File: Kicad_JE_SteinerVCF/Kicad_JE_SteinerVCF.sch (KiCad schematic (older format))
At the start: 36 parts

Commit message: Initial complete RevA sch
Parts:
- added C5: 1u, symbol Device:C
- added C6: 10u, symbol Device:CP
- added Q1: BC559, Package_TO_SOT_THT:TO-92_Inline, symbol Transistor_BJT:BC559
- added Q2: BC549, Package_TO_SOT_THT:TO-92_Inline, symbol Transistor_BJT:BC549
- added R2: 82k, symbol Device:R
- added R3: 3M3, symbol Device:R
- added R4: 18k, symbol Device:R
- added R5: 1k, symbol Device:R
- added R6, R7: 2k, symbol Device:R
- added RV3: 25k, symbol Device:R_POT_TRIM
- RV1: renamed from RV?; value R_POT -> 1k
- gave numbers to parts that had none: 30
- renumbered C3 to C2, C4 to C3, C2 to C4
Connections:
- wire segments 103 -> 135
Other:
- note added: "Driver"
- note added: "Q Adj"

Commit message: SMD sub sheet
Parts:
- added C?: CP, symbol Device:CP
- added P?: Doepfer_Power_10pin, Connectors_IDC:IDC-Header_2x05_Pitch2.54mm_Straight, symbol Eurorack:Doepfer_Power_10pin
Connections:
- wire segments 135 -> 160

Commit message: ERC, Footprints and Annotation in SCH
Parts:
- C101: renamed from C1; footprint (none) -> Capacitor_THT:C_Rect_L7.0mm_W2.0mm_P5.00mm
- C102: renamed from C2; footprint (none) -> Capacitor_THT:CP_Radial_D10.0mm_P5.00mm
- C103: renamed from C3; footprint (none) -> Capacitor_THT:CP_Radial_D10.0mm_P5.00mm
- C104: renamed from C4; footprint (none) -> Capacitor_THT:C_Rect_L7.0mm_W2.0mm_P5.00mm
- C105: renamed from C?; footprint (none) -> Capacitor_THT:CP_Radial_D10.0mm_P5.00mm
- C106: renamed from C5; footprint (none) -> Capacitor_THT:C_Rect_L7.0mm_W2.0mm_P5.00mm
- C107: renamed from C6; footprint (none) -> Capacitor_THT:CP_Radial_D10.0mm_P3.80mm
- C108: renamed from C7; footprint (none) -> Capacitor_THT:C_Rect_L7.0mm_W2.0mm_P5.00mm
- C109: renamed from C8; footprint (none) -> Capacitor_THT:C_Rect_L7.0mm_W2.0mm_P5.00mm
- C110: renamed from C9; footprint (none) -> Capacitor_THT:C_Rect_L7.0mm_W2.0mm_P5.00mm
- C111: renamed from C10; footprint (none) -> Capacitor_THT:CP_Radial_D10.0mm_P5.00mm
- J101: renamed from J1; footprint (none) -> AJ-Dropbox-Kicad:PJ301SM
- J102: renamed from J2; footprint (none) -> AJ-Dropbox-Kicad:PJ301SM
- J103: renamed from J3; footprint (none) -> AJ-Dropbox-Kicad:PJ301SM
- J104: renamed from J4; footprint (none) -> AJ-Dropbox-Kicad:PJ301SM
- J105: renamed from J5; footprint (none) -> AJ-Dropbox-Kicad:PJ301SM
- R101: renamed from R1; footprint (none) -> Resistor_THT:R_Axial_DIN0309_L9.0mm_D3.2mm_P12.70mm_Horizontal
- R102: renamed from R2; footprint (none) -> Resistor_THT:R_Axial_DIN0309_L9.0mm_D3.2mm_P12.70mm_Horizontal
- R103: renamed from R3; footprint (none) -> Resistor_THT:R_Axial_DIN0309_L9.0mm_D3.2mm_P12.70mm_Horizontal
- R104: renamed from R4; footprint (none) -> Resistor_THT:R_Axial_DIN0309_L9.0mm_D3.2mm_P12.70mm_Horizontal
- R105: renamed from R5; footprint (none) -> Resistor_THT:R_Axial_DIN0309_L9.0mm_D3.2mm_P12.70mm_Horizontal
- R106: renamed from R6; footprint (none) -> Resistor_THT:R_Axial_DIN0309_L9.0mm_D3.2mm_P12.70mm_Horizontal
- R107: renamed from R7; footprint (none) -> Resistor_THT:R_Axial_DIN0309_L9.0mm_D3.2mm_P12.70mm_Horizontal
- R108: renamed from R8; footprint (none) -> Resistor_THT:R_Axial_DIN0309_L9.0mm_D3.2mm_P12.70mm_Horizontal
- R109: renamed from R9; footprint (none) -> Resistor_THT:R_Axial_DIN0309_L9.0mm_D3.2mm_P12.70mm_Horizontal
- R110: renamed from R10; footprint (none) -> Resistor_THT:R_Axial_DIN0309_L9.0mm_D3.2mm_P12.70mm_Horizontal
- R111: renamed from R11; footprint (none) -> Resistor_THT:R_Axial_DIN0309_L9.0mm_D3.2mm_P12.70mm_Horizontal
- R112: renamed from R12; footprint (none) -> Resistor_THT:R_Axial_DIN0309_L9.0mm_D3.2mm_P12.70mm_Horizontal
- R113: renamed from R13; footprint (none) -> Resistor_THT:R_Axial_DIN0309_L9.0mm_D3.2mm_P12.70mm_Horizontal
- R114: renamed from R14; footprint (none) -> Resistor_THT:R_Axial_DIN0309_L9.0mm_D3.2mm_P12.70mm_Horizontal
- R115: renamed from R15; footprint (none) -> Resistor_THT:R_Axial_DIN0309_L9.0mm_D3.2mm_P12.70mm_Horizontal
- R116: renamed from R16; footprint (none) -> Resistor_THT:R_Axial_DIN0309_L9.0mm_D3.2mm_P12.70mm_Horizontal
- R117: renamed from R17; footprint (none) -> Resistor_THT:R_Axial_DIN0309_L9.0mm_D3.2mm_P12.70mm_Horizontal
- RV101: renamed from RV1; footprint (none) -> Potentiometer_THT:Potentiometer_Alps_RK09K_Single_Vertical
- RV102: renamed from RV2; footprint (none) -> Potentiometer_THT:Potentiometer_Alps_RK09K_Single_Vertical
- RV103: renamed from RV3; footprint (none) -> Potentiometer_THT:Potentiometer_Alps_RK09K_Single_Vertical
- gave numbers to parts that had none: 1
- renumbered D1 to D101, D2 to D102, D3 to D103, D4 to D104, D5 to D105, D6 to D106, D7 to D107, D8 to D108, Q1 to Q101, Q2 to Q102, Q3 to Q103, Q4 to Q104

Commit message: SMD section routed RevA
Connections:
- net labels added: +10V
- net labels removed: VCC
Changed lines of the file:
@@
 	0    1    1    0
-$EndComp
-$Comp
-L power:VCC #PWR0102
-U 1 1 5C434C5C
-P 4700 700
-F 0 "#PWR0102" H 4700 550 50  0001 C CNN
-F 1 "VCC" H 4717 873 50  0000 C CNN
-F 2 "" H 4700 700 50  0001 C CNN
-F 3 "" H 4700 700 50  0001 C CNN
-	1    4700 700
-	1    0    0    -1
 $EndComp
 Wire Wire Line
@@
 Wire Wire Line
 	2000 4850 2000 4750
-$Comp
-L power:VCC #PWR0109
-U 1 1 5C446275
-P 2000 4400
-F 0 "#PWR0109" H 2000 4250 50  0001 C CNN
-F 1 "VCC" H 2017 4573 50  0000 C CNN
-F 2 "" H 2000 4400 50  0001 C CNN
-F 3 "" H 2000 4400 50  0001 C CNN
-	1    2000 4400
-	1    0    0    -1
-$EndComp
 Wire Wire Line
 	2000 4450 2000 4400
@@
 F 3 "http://www.fairchildsemi.com/ds/BC/BC547.pdf" H 3350 2450 50  0001 L CNN
 	1    3350 2450
-	1    0    0    -1
-$EndComp
-$Comp
-L power:VCC #PWR0106
-U 1 1 5C480942
-P 2800 1800
-F 0 "#PWR0106" H 2800 1650 50  0001 C CNN
-F 1 "VCC" H 2817 1973 50  0000 C CNN
-F 2 "" H 2800 1800 50  0001 C CNN
-F 3 "" H 2800 1800 50  0001 C CNN
-	1    2800 1800
 	1    0    0    -1
 $EndComp
@@
 $EndComp
 Connection ~ 2450 1400
+$Comp
+L power:+10V #PWR0102
+U 1 1 5C60D9FE
+P 2000 4400
+F 0 "#PWR0102" H 2000 4250 50  0001 C CNN
+F 1 "+10V" H 2015 4573 50  0000 C CNN
+F 2 "" H 2000 4400 50  0001 C CNN
+F 3 "" H 2000 4400 50  0001 C CNN
+	1    2000 4400
+	1    0    0    -1
+$EndComp
+$Comp
+L power:+10V #PWR0106
+U 1 1 5C60DB41
+P 4700 700
+F 0 "#PWR0106" H 4700 550 50  0001 C CNN
+F 1 "+10V" H 4715 873 50  0000 C CNN
+F 2 "" H 4700 700 50  0001 C CNN
+F 3 "" H 4700 700 50  0001 C CNN
+	1    4700 700
+	1    0    0    -1
+$EndComp
+$Comp
+L power:+10V #PWR0109
+U 1 1 5C60DF5D
+P 2800 1800
+F 0 "#PWR0109" H 2800 1650 50  0001 C CNN
+F 1 "+10V" H 2815 1973 50  0000 C CNN
+F 2 "" H 2800 1800 50  0001 C CNN
+F 3 "" H 2800 1800 50  0001 C CNN
+	1    2800 1800
+	1    0    0    -1
+$EndComp
 $EndSCHEMATC

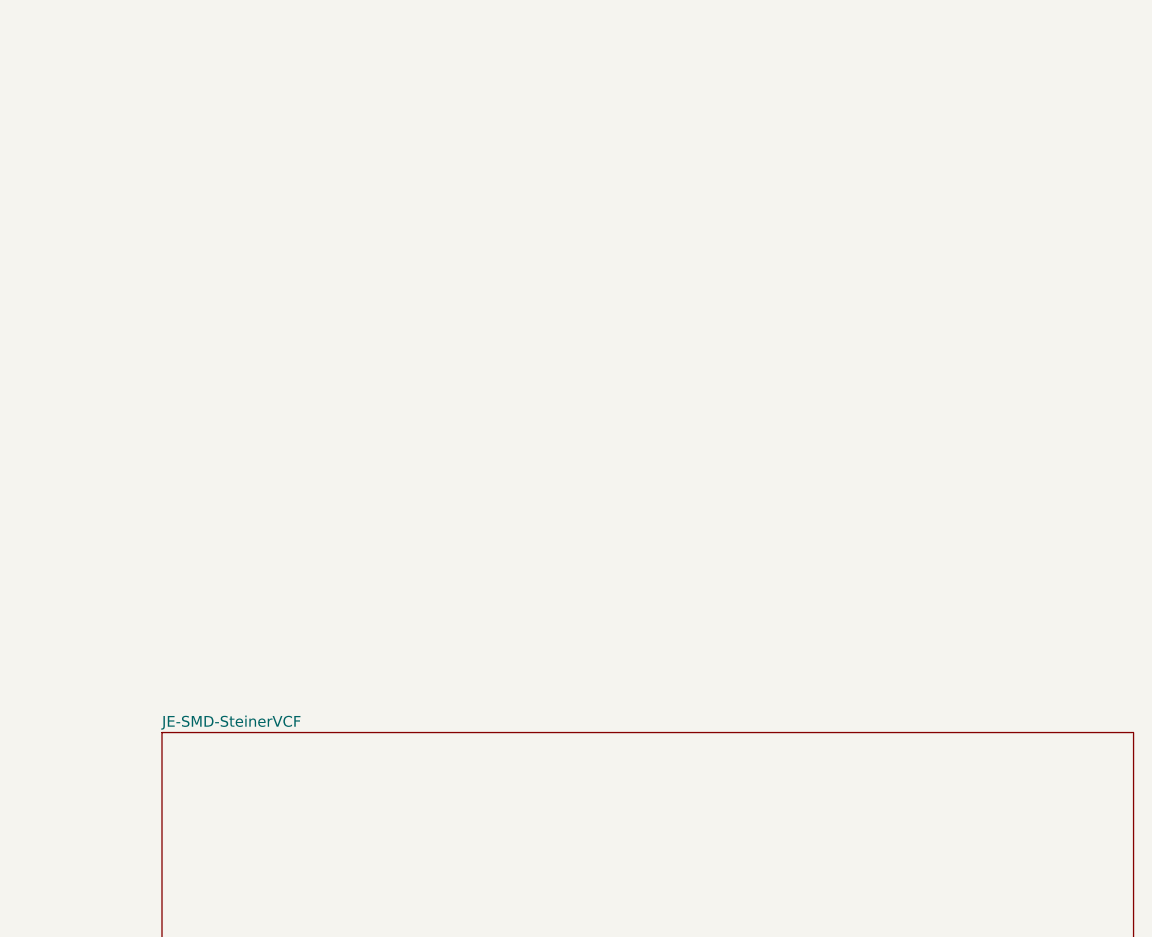
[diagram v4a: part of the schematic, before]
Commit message: ICL8083 VCO added sch, ERC and footprints
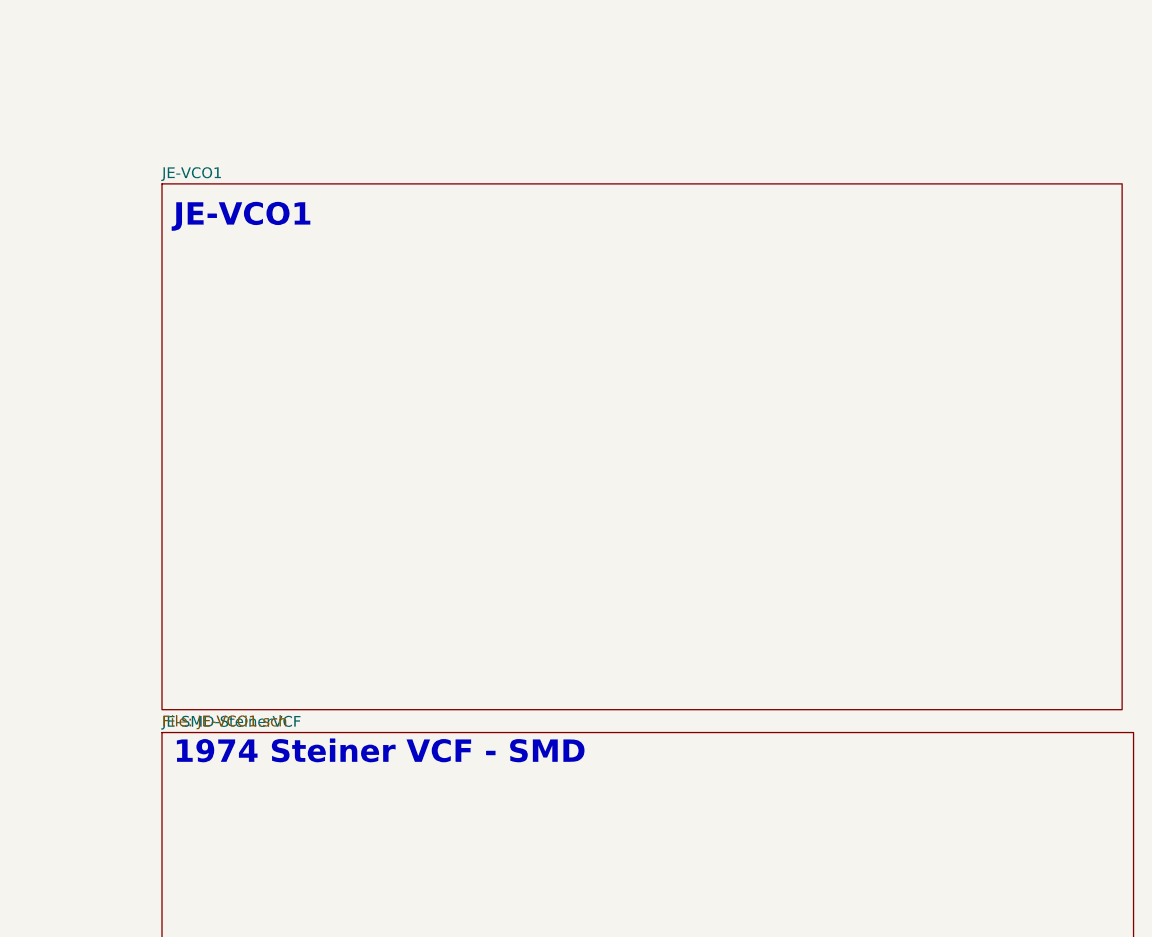
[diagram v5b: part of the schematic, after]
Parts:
- J101: value AudioJack2_SwitchT -> HP
- J102: value AudioJack2_SwitchT -> BP
- J103: value AudioJack2_SwitchT -> LP
- J104: value AudioJack2_SwitchT -> Out
- J105: value AudioJack2_SwitchT -> CV
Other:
- note added: "1974 Steiner VCF - SMD"
- note added: "JE-VCO1"
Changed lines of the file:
@@
 $Descr A4 11693 8268
 encoding utf-8
-Sheet 1 2
+Sheet 1 3
 Title "JE-Steiner-VCF"
 Date "2019-01-19"
@@
 P 950 1900
 F 0 "J101" H 980 2225 50  0000 C CNN
-F 1 "AudioJack2_SwitchT" H 980 2134 50  0000 C CNN
+F 1 "HP" H 980 2134 50  0000 C CNN
 F 2 "AJ-Dropbox-Kicad:PJ301SM" H 950 1900 50  0001 C CNN
 F 3 "~" H 950 1900 50  0001 C CNN
@@
 P 950 2300
 F 0 "J102" H 980 2625 50  0000 C CNN
-F 1 "AudioJack2_SwitchT" H 980 2534 50  0000 C CNN
+F 1 "BP" H 980 2534 50  0000 C CNN
 F 2 "AJ-Dropbox-Kicad:PJ301SM" H 950 2300 50  0001 C CNN
 F 3 "~" H 950 2300 50  0001 C CNN
@@
 P 950 2750
 F 0 "J103" H 980 3075 50  0000 C CNN
-F 1 "AudioJack2_SwitchT" H 980 2984 50  0000 C CNN
+F 1 "LP" H 980 2984 50  0000 C CNN
 F 2 "AJ-Dropbox-Kicad:PJ301SM" H 950 2750 50  0001 C CNN
 F 3 "~" H 950 2750 50  0001 C CNN
@@
 P 950 3200
 F 0 "J104" H 980 3525 50  0000 C CNN
-F 1 "AudioJack2_SwitchT" H 980 3434 50  0000 C CNN
+F 1 "Out" H 980 3434 50  0000 C CNN
 F 2 "AJ-Dropbox-Kicad:PJ301SM" H 950 3200 50  0001 C CNN
 F 3 "~" H 950 3200 50  0001 C CNN
@@
 P 950 3600
 F 0 "J105" H 980 3925 50  0000 C CNN
-F 1 "AudioJack2_SwitchT" H 980 3834 50  0000 C CNN
+F 1 "CV" H 980 3834 50  0000 C CNN
 F 2 "AJ-Dropbox-Kicad:PJ301SM" H 950 3600 50  0001 C CNN
 F 3 "~" H 950 3600 50  0001 C CNN
@@
 	1    0    0    -1
 $EndComp
+Text Notes 6950 4100 0    98   ~ 20
+1974 Steiner VCF - SMD
+$Sheet
+S 6900 1550 4200 2300
+U 5C618010
+F0 "JE-VCO1" 47
+F1 "JE-VCO1.sch" 47
+$EndSheet
+Text Notes 6950 1750 0    98   ~ 20
+JE-VCO1
 $EndSCHEMATC
